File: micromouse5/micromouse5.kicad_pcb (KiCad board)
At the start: 2 copper layers, 75 x 105 mm, 71 parts, among them J1 Conn_01x06_Pin, J2 Conn_01x06_Pin, J3 JST 2, J4 JST 1, J5 Conn_01x04_Pin, Q1 IR Receiver, Q2 IR Receiver, Q3 IR Receiver, Q4 IR Receiver, SW1 Button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

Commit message: pcb work
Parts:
- moved R5 127.7 mm to (177.0, 69.9)
- moved C2 121.3 mm to (152.6, 122.9)
- moved C3 115.9 mm to (141.9, 130.4), turned to 180 degrees
- moved R8 115.1 mm to (198.1, 79.4)
- moved C1 100.6 mm to (160.5, 122.9), turned to 180 degrees
- moved R7 97.8 mm to (205.0, 79.4)
- moved C23 97.4 mm to (153.5, 85.4), turned to 180 degrees
- moved R13 96.7 mm to (146.5, 91.9)
- moved C25 95.9 mm to (159.9, 85.4), turned to 180 degrees
- moved R6 90.5 mm to (198.1, 73.9)
- moved C10 86.6 mm to (139.9, 79.4)
- moved C14 86.6 mm to (139.9, 85.2)
- moved C4 84.2 mm to (142.4, 122.9)
- moved R17 83.8 mm to (160.0, 91.9), turned to 180 degrees
- moved C13 80.2 mm to (153.5, 91.9)
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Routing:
- net 3V3: track 72.3 -> 310.9 mm, vias 0 -> 1
- net VCC: track 0.00 -> 126.3 mm, vias 0 -> 2
- net NRST: track 0.00 -> 41.7 mm
- net MGND: track 0.00 -> 40.8 mm
- net Net-(J3-Pad1): track 0.00 -> 27.6 mm
- net Net-(R19-Pad2): track 0.00 -> 17.3 mm
- net Net-(D5-K): track 0.00 -> 12.0 mm
- net Net-(J3-Pad2): track 0.00 -> 8.83 mm
- net Net-(C24-Pad2): track 0.00 -> 6.77 mm

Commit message: PCB work
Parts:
- moved R7 14.1 mm to (192.0, 74.0)
- moved R13 13.7 mm to (160.2, 91.9), turned to 180 degrees
- moved C7 13.4 mm to (205.0, 73.9)
- moved R17 13.0 mm to (147.0, 92.0)
- moved R15 5.41 mm to (153.0, 74.0), turned to 180 degrees
- moved R16 5.00 mm to (154.0, 79.0)
- moved R12 4.89 mm to (168.0, 65.0)
- moved R11 4.61 mm to (168.0, 70.0)
- moved D5 2.00 mm to (144.0, 137.4)
- moved U2 2.00 mm to (146.0, 147.9)
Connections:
- C1 pad 2: VCC -> 3V3
- C2 pad 1: VCC -> 3V3
- C3 pad 2: VCC -> 3V3
- C4 pad 1: VCC -> 3V3
- C5 pad 1: VCC -> 3V3
- R11 pad 2: unconnected-(R11-Pad2) -> Net-(R11-Pad2)
- R15 pad 2: unconnected-(R15-Pad2) -> Net-(R13-Pad2)
- R3 pad 2: unconnected-(R3-Pad2) -> Net-(R2-Pad2)
- R7 pad 2: unconnected-(R7-Pad2) -> Net-(R5-Pad2)
- R9 pad 2: Net-(R9-Pad2) -> Net-(R11-Pad2)
- SW2 pad 1: VCC -> 3V3
- U1 pad 20: VCC -> 3V3
- U2 pad 3: VCC -> 3V3
- U5 pad 1: Net-(R9-Pad2) -> Net-(R11-Pad2)
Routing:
- net 3V3: track 310.9 -> 471.9 mm, vias 1 -> 3
- net VCC: track 126.3 -> 0.00 mm, vias 2 -> 0
- net NRST: track 41.7 -> 143.1 mm, vias 0 -> 1
- net Net-(U7-PB2): track 0.00 -> 32.6 mm
- net Net-(Q3-Pad1): track 0.00 -> 22.9 mm
- net Net-(R5-Pad2): track 0.00 -> 21.8 mm
- net Net-(Q1-Pad1): track 0.00 -> 20.5 mm
- net Net-(U7-VCAP_1): track 0.00 -> 15.9 mm
- net PC5: track 0.00 -> 14.3 mm
- net Net-(R11-Pad2): track 0.00 -> 11.0 mm
- net Net-(Q2-Pad1): track 0.00 -> 9.56 mm
- net Net-(R13-Pad2): track 0.00 -> 9.40 mm
- net Net-(Q4-Pad1): track 0.00 -> 8.17 mm
- net Net-(D3-PadC): track 0.00 -> 8.02 mm
- net Net-(D5-K): track 12.0 -> 11.2 mm

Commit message: Update micromouse5.kicad_pcb
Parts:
- moved R5 2.23 mm to (179.2, 69.9)
- moved R3 1.73 mm to (179.0, 65.4)
- moved R14 1.00 mm to (146.0, 74.0), turned to 180 degrees
- turned R18 to -90 degrees
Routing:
- net Net-(R11-Pad2): track 11.0 -> 29.3 mm, vias 0 -> 2
- net Net-(U7-BOOT0): track 0.00 -> 16.7 mm, vias 0 -> 2
- net Net-(U7-PB2): track 32.6 -> 34.3 mm
- net PC5: track 14.3 -> 15.6 mm
- net Net-(Q4-Pad1): track 8.17 -> 7.36 mm
- net 3V3: track 471.9 -> 471.4 mm

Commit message: more vias
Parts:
- moved Motor1 1.89 mm to (143.0, 102.5)
- moved Motor2 1.39 mm to (202.0, 106.0)
- moved C15 1.33 mm to (186.5, 91.9)
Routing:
- net SWDIO: track 0.00 -> 77.2 mm, vias 0 -> 4
- net PC4: track 0.00 -> 35.9 mm, vias 0 -> 2
- net ML2: track 0.00 -> 29.1 mm
- net PC2: track 0.00 -> 27.8 mm, vias 0 -> 4
- net PA9: track 0.00 -> 27.0 mm, vias 0 -> 2
- net Net-(R13-Pad2): track 9.40 -> 31.8 mm, vias 0 -> 2
- net PA0: track 0.00 -> 22.3 mm, vias 0 -> 2
- net MR2: track 0.00 -> 20.9 mm
- net ML1: track 0.00 -> 19.3 mm
- net Net-(R2-Pad2): track 0.00 -> 18.8 mm, vias 0 -> 2
- net 3V3: track 471.4 -> 484.2 mm, vias 3 -> 5
- net Net-(U7-VCAP_2): track 0.00 -> 8.98 mm

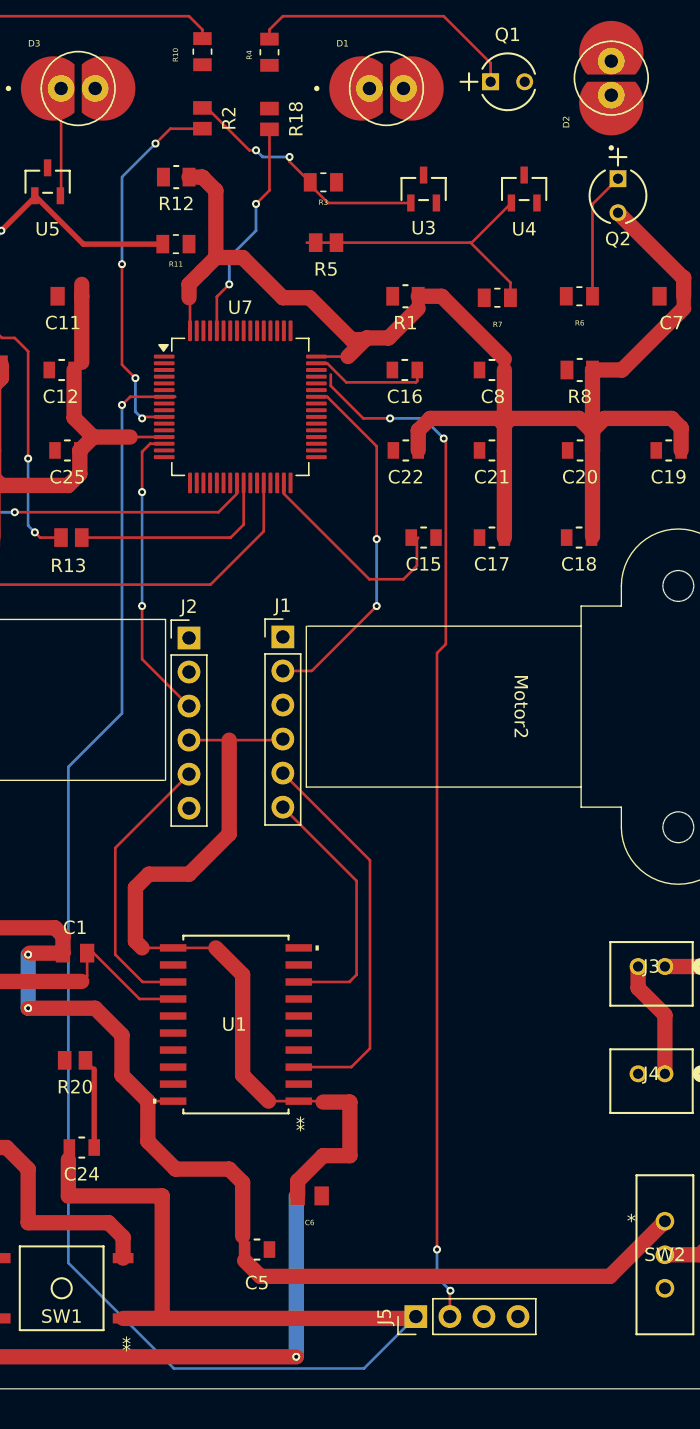
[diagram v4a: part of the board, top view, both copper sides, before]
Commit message: More vias and microcontroller connections
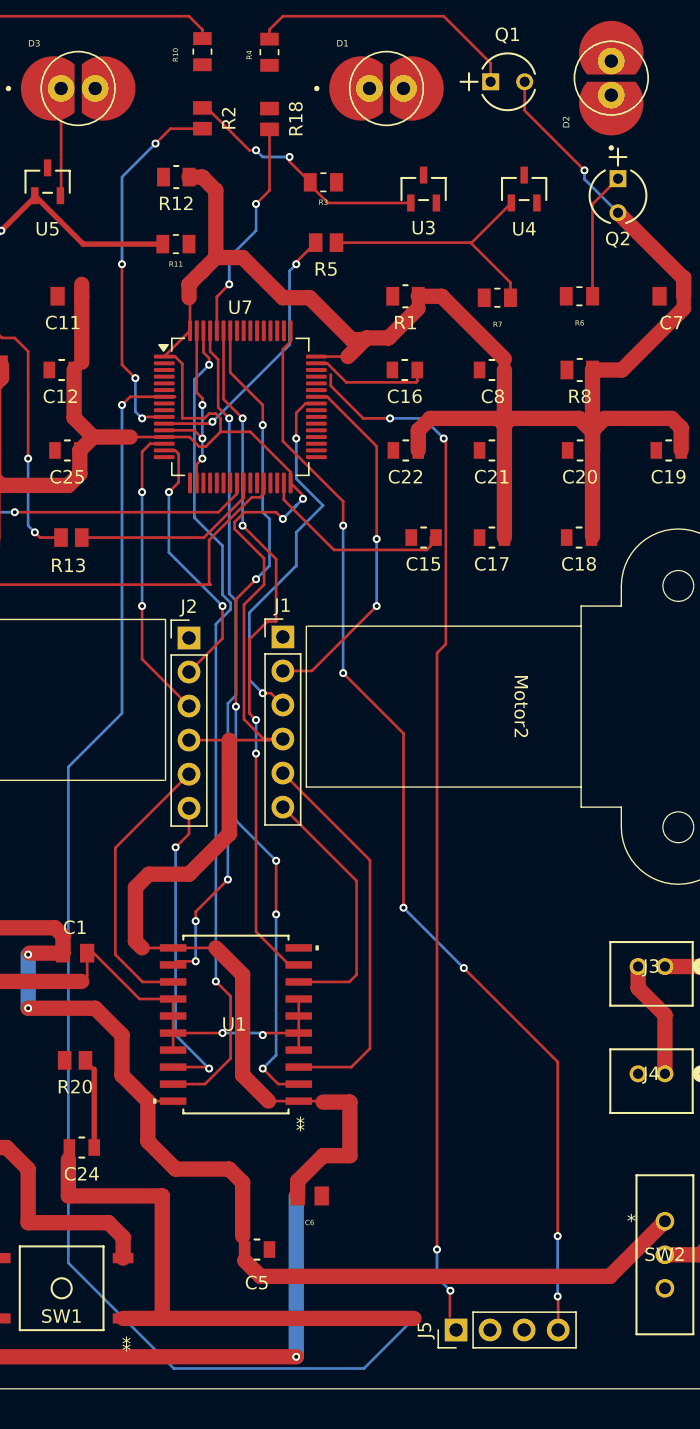
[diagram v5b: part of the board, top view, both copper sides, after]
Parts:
- moved J5 3.16 mm to (188.9, 151.0)
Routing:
- net SWCLK: track 0.00 -> 83.3 mm, vias 0 -> 6
- net 3V3: track 484.2 -> 549.8 mm, vias 5 -> 8
- net PB6: track 0.00 -> 62.1 mm, vias 0 -> 6
- net PB9: track 0.00 -> 62.0 mm, vias 0 -> 2
- net PB7: track 0.00 -> 52.1 mm, vias 0 -> 4
- net PB8: track 0.00 -> 50.9 mm, vias 0 -> 4
- net PA8: track 0.00 -> 28.1 mm, vias 0 -> 2
- net MR1: track 0.00 -> 23.6 mm, vias 0 -> 2
- net PA1: track 0.00 -> 20.4 mm, vias 0 -> 2
- net PC3: track 0.00 -> 20.2 mm, vias 0 -> 2
- net MGND: track 40.8 -> 57.9 mm, vias 0 -> 2
- net GND: track 0.00 -> 14.8 mm, vias 0 -> 3
- net Net-(R5-Pad2): track 21.8 -> 19.6 mm
- net PC5: track 15.6 -> 14.4 mm
- net Net-(U7-VCAP_1): track 15.9 -> 14.9 mm

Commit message: finished connections
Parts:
- moved C15 1.02 mm to (186.0, 91.0), turned to 180 degrees
- moved C16 0.39 mm to (185.1, 79.0), turned to 180 degrees
- turned C7 to 180 degrees
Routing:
- net Net-(D2-PadA): track 0.00 -> 27.3 mm, vias 0 -> 2
- net Net-(D4-PadA): track 0.00 -> 24.4 mm
- net Net-(D4-PadC): track 0.00 -> 19.0 mm
- net Net-(D1-PadA): track 0.00 -> 17.7 mm, vias 0 -> 2
- net Net-(D2-PadC): track 0.00 -> 14.4 mm, vias 0 -> 2
- net Net-(D1-PadC): track 0.00 -> 14.2 mm
- net Net-(D3-PadA): track 0.00 -> 8.72 mm
- net Net-(U7-VCAP_2): track 8.98 -> 5.54 mm
- net Net-(U7-VCAP_1): track 14.9 -> 12.6 mm
- net 3V3: track 549.8 -> 548.2 mm
- net SWDIO: track 77.2 -> 78.5 mm, vias 4 -> 1
- net SWCLK: vias 6 -> 4

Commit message: updates
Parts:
- moved C2 36.9 mm to (189.1, 127.9)
- moved C1 28.7 mm to (189.2, 122.0)
- moved C4 19.9 mm to (158.9, 134.0), turned to 180 degrees
- moved C3 17.2 mm to (159.0, 128.0), turned to 0 degrees
- moved D5 12.4 mm to (144.0, 125.0)
- moved R20 11.0 mm to (153.0, 139.0)
- moved R21 8.48 mm to (144.0, 130.9)
- moved R19 8.46 mm to (144.0, 137.4)
- moved C24 4.31 mm to (165.0, 139.0), turned to 180 degrees
- moved C5 1.41 mm to (173.1, 144.0)
- moved J5 1.00 mm to (188.9, 150.0)
- moved SW1 0.89 mm to (159.5, 147.0)
- moved U2 0.89 mm to (146.0, 147.0)
- moved R10 0.34 mm to (170.0, 56.0)
- moved R4 0.34 mm to (175.0, 56.0)
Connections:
- C1 pad 1: MGND -> GND
- C1 pad 2: 3V3 -> VCC
- C15 pad 2: Net-(U7-VCAP_1) -> 3V3
- C2 pad 1: 3V3 -> VCC
- C2 pad 2: MGND -> GND
- C3 pad 1: MGND -> GND
- C3 pad 2: 3V3 -> VCC
- C4 pad 1: 3V3 -> VCC
- C4 pad 2: MGND -> GND
- J1 pad 2: PA9 -> 3V3
- U1 pad 14: MGND -> GND
- U1 pad 15: MGND -> GND
- U1 pad 16: MGND -> GND
- U1 pad 17: MGND -> GND
- U1 pad 20: 3V3 -> VCC
- U1 pad 4: MGND -> GND
- U1 pad 5: MGND -> GND
- U1 pad 6: MGND -> GND
- U1 pad 7: MGND -> GND
- U7 pad 30: unconnected-(U7-PB11-Pad30) -> 3V3
- U7 pad 31: Net-(U7-VCAP_1) -> 3V3
- U7 pad 42: PA9 -> 3V3
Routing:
- net GND: track 14.8 -> 91.3 mm, vias 3 -> 30
- net VCC: track 0.00 -> 73.5 mm, vias 0 -> 2
- net MGND: track 57.9 -> 0.00 mm, vias 2 -> 0
- net PA9: track 27.0 -> 0.00 mm, vias 2 -> 0
- net Net-(U7-VCAP_1): track 12.6 -> 0.00 mm
- net 3V3: track 548.2 -> 538.7 mm, vias 8 -> 7
- net Net-(R19-Pad2): track 17.3 -> 23.8 mm
- net Net-(D5-K): track 11.2 -> 6.76 mm
- net Net-(C24-Pad2): track 6.77 -> 10.3 mm
- net NRST: track 143.1 -> 139.6 mm, vias 1 -> 2
- net ML2: track 29.1 -> 32.2 mm, vias 0 -> 2
- net Net-(R13-Pad2): track 31.8 -> 30.3 mm
- net PA1: track 20.4 -> 21.9 mm
- net PC4: track 35.9 -> 37.3 mm
- net Net-(J3-Pad2): track 8.83 -> 10.1 mm
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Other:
- board size 75 x 105 mm -> 75 x 101 mm

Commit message: Revised changes
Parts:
- moved C19 45.4 mm to (160.0, 93.0)
- moved C17 36.4 mm to (159.9, 74.0)
- moved C18 31.0 mm to (167.1, 92.0)
- moved C22 26.0 mm to (159.9, 79.0)
- moved C12 15.9 mm to (146.0, 71.0)
- moved C9 12.1 mm to (138.9, 76.0)
- moved C20 9.09 mm to (191.9, 92.0)
- moved C13 9.02 mm to (145.9, 87.0)
- moved C21 7.77 mm to (186.0, 80.0)
- moved C11 6.84 mm to (153.9, 71.0)
- moved R13 6.32 mm to (154.0, 93.0)
- moved C16 6.07 mm to (186.0, 85.0)
- moved C6 3.66 mm to (180.1, 144.0)
- moved R15 2.23 mm to (154.0, 76.0)
- moved C14 2.02 mm to (139.0, 87.0)
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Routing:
- net PC5: track 15.0 -> 26.4 mm
- net PC4: track 37.3 -> 42.3 mm
- net Net-(U7-VCAP_2): track 5.54 -> 10.2 mm
- net Net-(R13-Pad2): track 30.3 -> 34.8 mm
- net Net-(Q4-Pad1): track 6.95 -> 9.55 mm
- net Net-(R11-Pad2): track 29.9 -> 31.6 mm
- net Net-(U7-PB2): track 34.9 -> 36.5 mm
- net Net-(D4-PadA): track 23.8 -> 25.2 mm
- net 3V3: track 538.7 -> 539.7 mm
- net PA0: track 23.2 -> 23.8 mm
- net PA1: track 21.9 -> 21.3 mm
- net GND: track 91.3 -> 91.4 mm, vias 30 -> 37
